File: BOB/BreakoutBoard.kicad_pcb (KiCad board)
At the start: 2 copper layers, 173 x 99 mm, 23 parts, among them J10 Conn_01x04, J11 Conn_01x02, J12 Conn_01x02, J13 Conn_01x04, J14 Conn_01x04, J15 Conn_01x06, J16 Conn_01x08, J17 Conn_01x08, J2 Conn_01x08, J3 1706013, J4 Conn_01x06, J5 Conn_01x08, J6 Conn_01x08, J7 Conn_01x08, J9 Conn_01x04

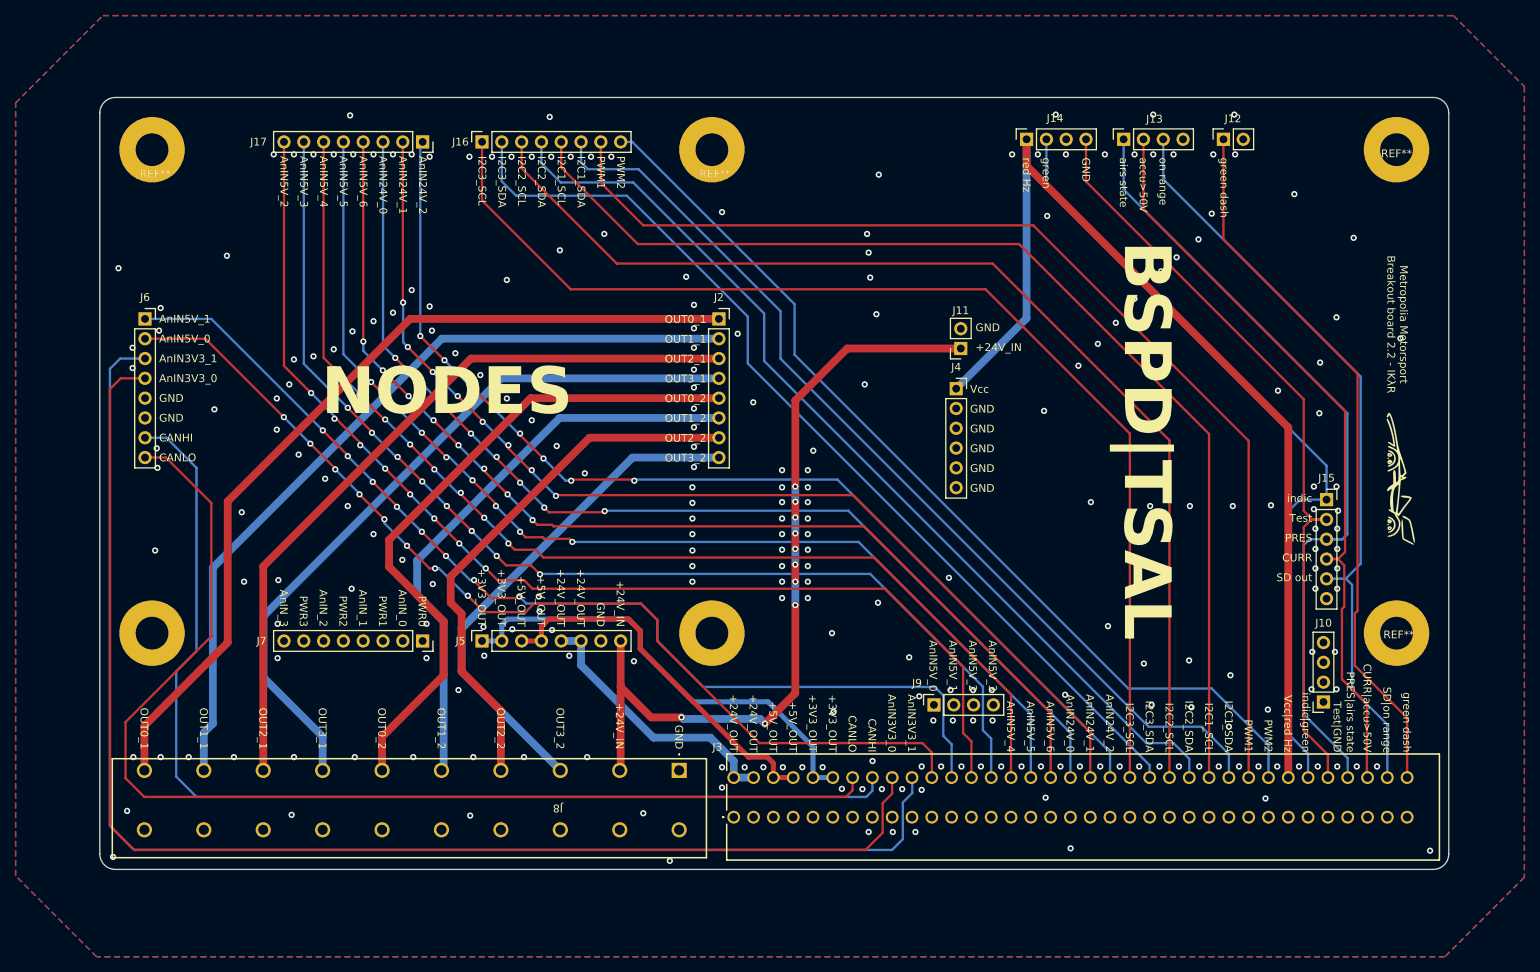
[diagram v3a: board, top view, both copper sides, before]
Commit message: v2.2.3
- New layout
- Removed from connectors:
* 2x +24V_OUT
* 1x +3V3_OUT
* 1x +5V_OUT
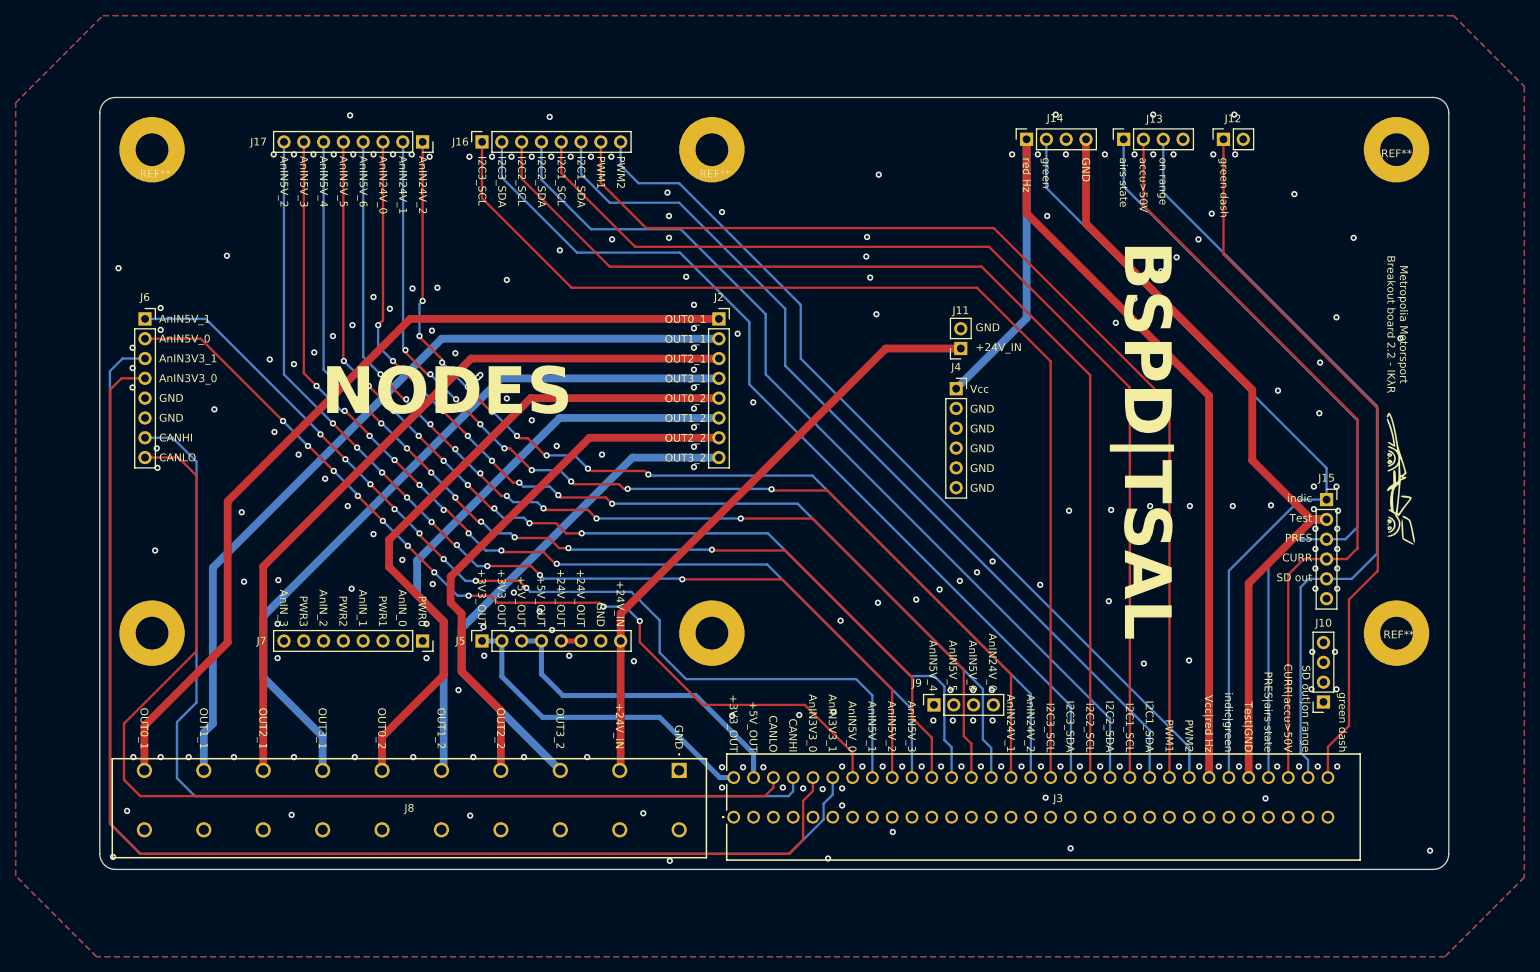
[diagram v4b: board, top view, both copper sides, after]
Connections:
- J3 pad 10: /+3V3_OUT -> /AnIN3V3_0
- J3 pad 12: /+3V3_OUT -> /AnIN3V3_1
- J3 pad 14: /CANLO -> /AnIN5V_0
- J3 pad 16: /CANHI -> /AnIN5V_1
- J3 pad 18: /AnIN3V3_0 -> /AnIN5V_2
- J3 pad 2: /+24V_OUT -> /+3V3_OUT
- J3 pad 20: /AnIN3V3_1 -> /AnIN5V_3
- J3 pad 22: /AnIN5V_0 -> /AnIN5V_4
- J3 pad 24: /AnIN5V_1 -> /AnIN5V_5
- J3 pad 26: /AnIN5V_2 -> /AnIN5V_6
- J3 pad 28: /AnIN5V_3 -> /AnIN24V_0
- J3 pad 30: /AnIN5V_4 -> /AnIN24V_1
- J3 pad 32: /AnIN5V_5 -> /AnIN24V_2
- J3 pad 34: /AnIN5V_6 -> /I2C3_SCL
- J3 pad 36: /AnIN24V_0 -> /I2C3_SDA
- J3 pad 38: /AnIN24V_1 -> /I2C2_SCL
- J3 pad 4: /+24V_OUT -> /+5V_OUT
- J3 pad 40: /AnIN24V_2 -> /I2C2_SDA
- J3 pad 42: /I2C3_SCL -> /I2C1_SCL
- J3 pad 44: /I2C3_SDA -> /I2C1_SDA
- J3 pad 46: /I2C2_SCL -> /PWM1
- J3 pad 48: /I2C2_SDA -> /PWM2
- J3 pad 50: /I2C1_SCL -> /Vcc / red Hz
- J3 pad 52: /I2C1_SDA -> /indic / green
- J3 pad 54: /PWM1 -> /Test / GND
- J3 pad 56: /PWM2 -> /PRES / airs state
- J3 pad 58: /Vcc / red Hz -> /CURR / accu>50V
- J3 pad 6: /+5V_OUT -> /CANLO
- J3 pad 60: /indic / green -> /SD out / on range
- J3 pad 62: /Test / GND -> /green dash
- J3 pad 8: /+5V_OUT -> /CANHI
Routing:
- net /+24V_OUT: track 35.0 -> 2.54 mm
- net /Vin: track 104.2 -> 77.9 mm, vias 10 -> 0
- net /+3V3_OUT: track 59.4 -> 42.2 mm
- net /AnIN3V3_1: track 175.6 -> 164.0 mm
- net /AnIN5V_0: track 129.0 -> 117.6 mm, vias 8 -> 10
- net /AnIN5V_2: track 146.9 -> 135.9 mm, vias 8 -> 9
- net /CANLO: track 147.0 -> 136.3 mm
- net /AnIN5V_3: track 144.9 -> 134.5 mm, vias 8 -> 9
- net /CANHI: track 141.3 -> 131.5 mm
- net /AnIN5V_4: track 144.7 -> 135.1 mm, vias 8 -> 9
- net /AnIN3V3_0: track 170.0 -> 160.4 mm
- net /AnIN5V_1: track 135.3 -> 126.7 mm
- net /AnIN5V_5: track 142.9 -> 134.6 mm, vias 8 -> 9
- net /PWM2: track 123.1 -> 114.8 mm
- net /PWM1: track 145.2 -> 137.9 mm
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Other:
- board text added: "SD out|on range"
- board text removed: "SD|on range"
